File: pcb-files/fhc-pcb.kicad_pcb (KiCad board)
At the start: 2 copper layers, 133.3 x 63.5 mm, 20 parts, among them J1 Screw_Terminal_01x02, SW1 SW_Push_Dual, SW2 SW_Push_Dual, SW3 SW_Push_Dual, SW4 SW_Push_Dual, SW5 SW_Push_Dual, U1 WeMos_D1_mini

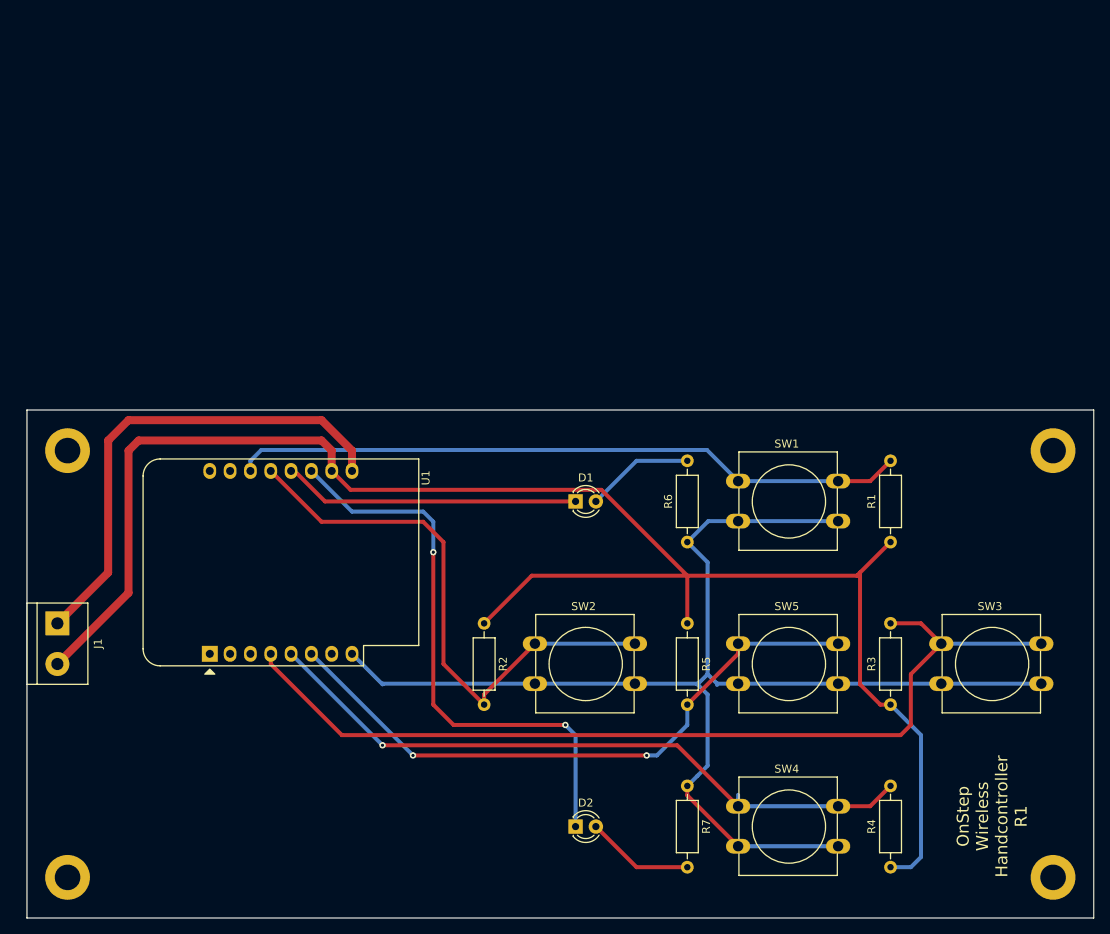
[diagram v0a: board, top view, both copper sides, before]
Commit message: Updated PCB with regulator and 9V battery
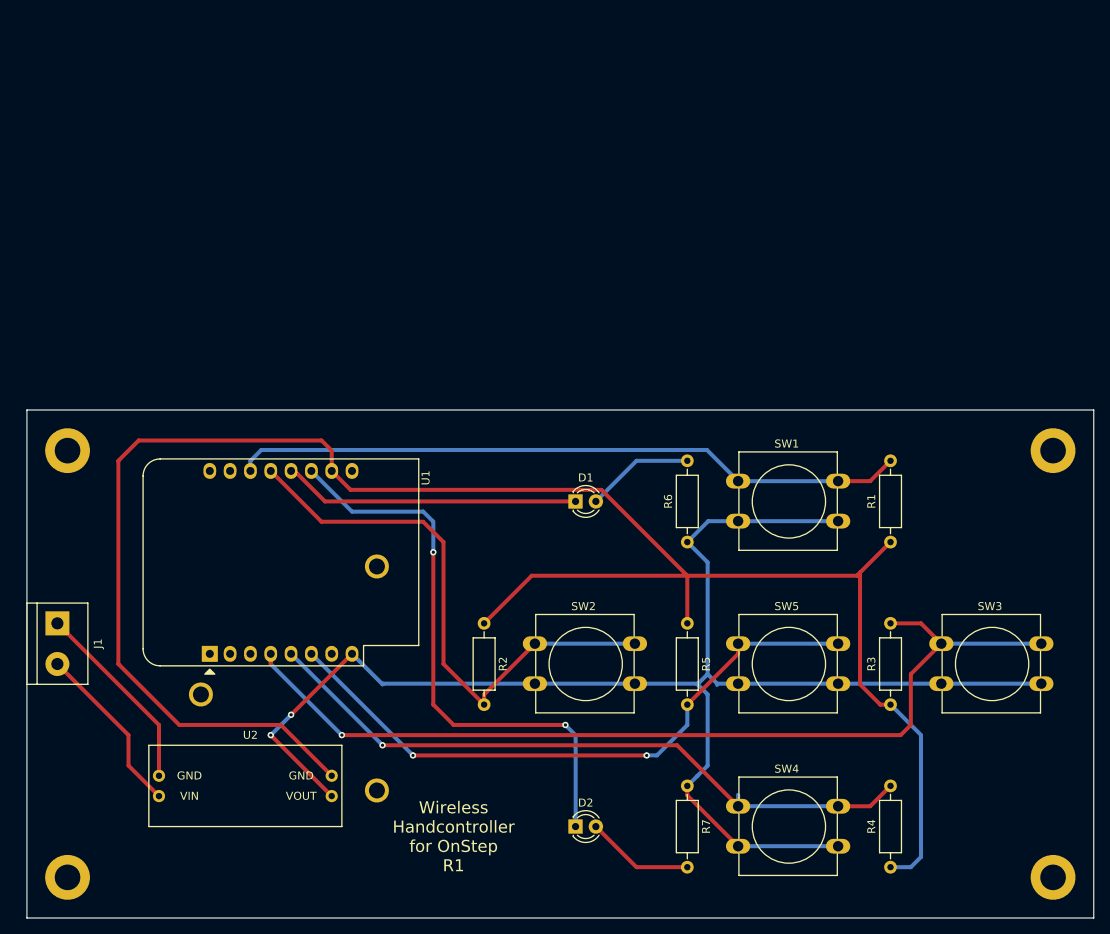
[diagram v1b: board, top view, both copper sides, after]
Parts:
- added REF**: 9V_Batterypack, Personal Library:9V_Batterypack, F.Cu at (127.0, 99.1)
- added U2: AMS1117_Shield_AZDelivery, Personal Library:AMS1117_Shield_AZDelivery, F.Cu at (123.2, 110.5)
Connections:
- J1 pad 1: +5V -> Net-(J1-Pad1)
- J1 pad 2: GND -> Net-(J1-Pad2)
- R1 pad 1: GND -> +9V
- R2 pad 1: GND -> +9V
- R3 pad 1: GND -> +9V
- R4 pad 1: GND -> +9V
- R5 pad 1: GND -> +9V
- U1 pad 10: GND -> +9V
- U1 pad 9: +5V -> Net-(U1-Pad9)
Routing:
- net +9V: track 0.00 -> 243.3 mm
- net GND: track 214.0 -> 0.00 mm
- net +5V: track 61.1 -> 0.00 mm
- net Net-(R6-Pad1): track 163.5 -> 188.6 mm, vias 0 -> 2
- net Net-(J1-Pad1): track 0.00 -> 24.3 mm
- net Net-(J1-Pad2): track 0.00 -> 21.8 mm
- net Net-(R3-Pad2): track 117.1 -> 118.4 mm, vias 0 -> 1
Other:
- board text added: "Wireless Handcontroller for OnStep R1"
- board text removed: "OnStep Wireless Handcontroller R1"

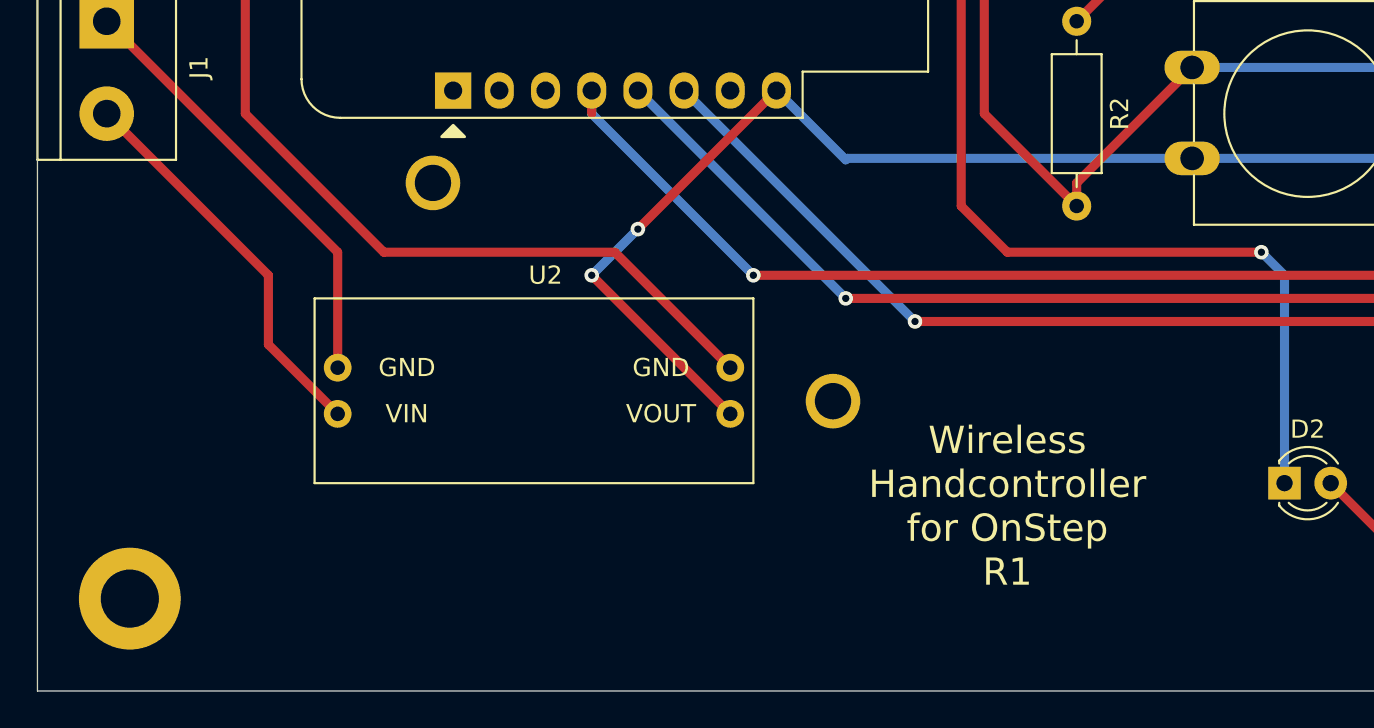
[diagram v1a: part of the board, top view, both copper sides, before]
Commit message: Added power switch
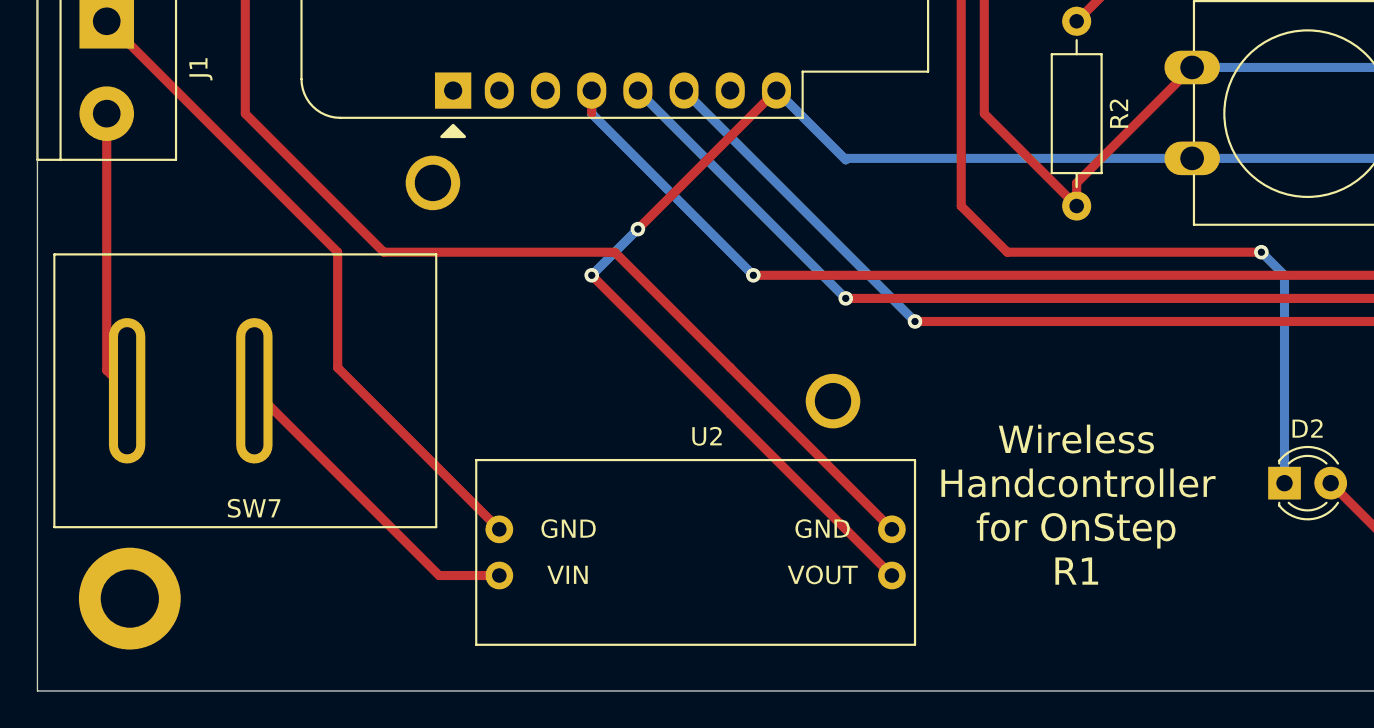
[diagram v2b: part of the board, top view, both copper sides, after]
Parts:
- added SW7: SW_Push, Personal Library:Wippschalter, F.Cu at (106.7, 110.5)
- moved U2 12.6 mm to (132.1, 119.4)
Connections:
- U2 pad 1: Net-(J1-Pad2) -> Net-(SW7-Pad2)
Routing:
- net Net-(SW7-Pad2): track 0.00 -> 17.7 mm
- net Net-(R6-Pad1): track 188.6 -> 201.2 mm
- net +9V: track 243.3 -> 255.9 mm
- net Net-(J1-Pad1): track 24.3 -> 36.9 mm
- net Net-(J1-Pad2): track 21.8 -> 15.7 mm

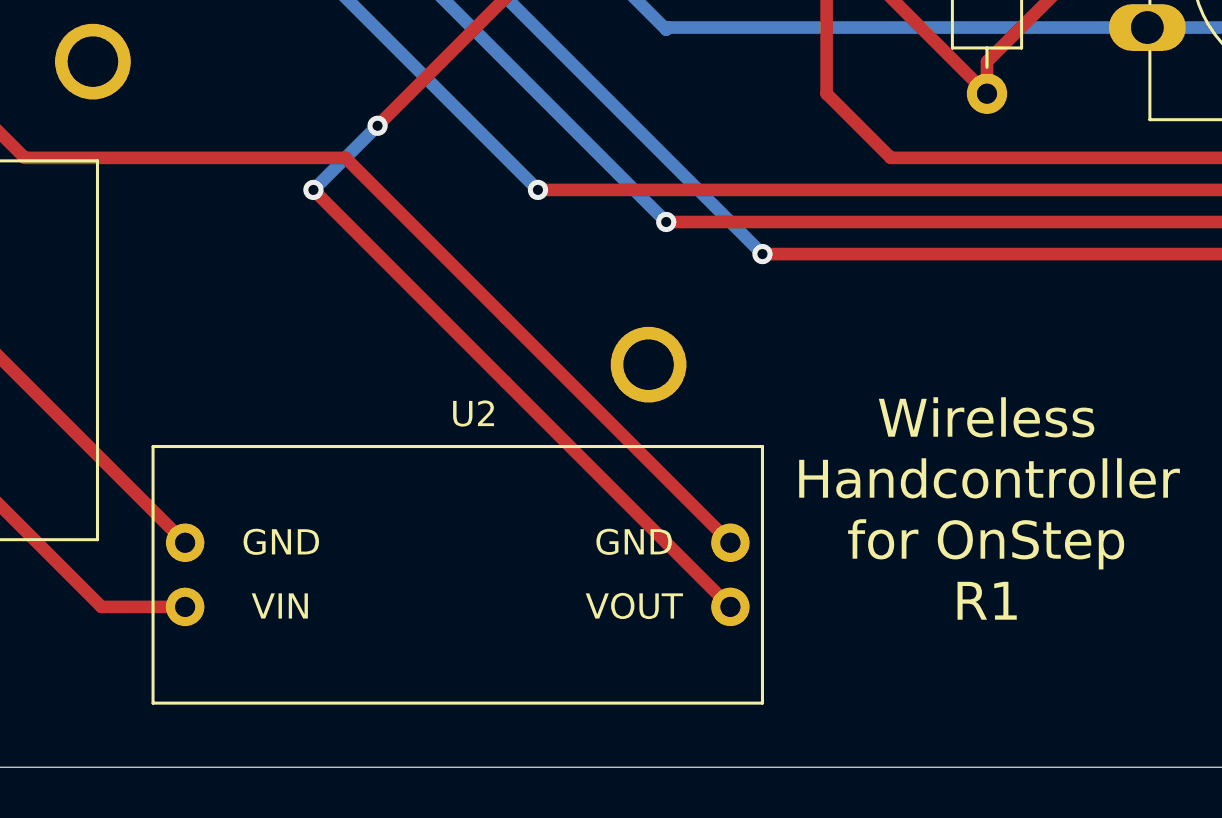
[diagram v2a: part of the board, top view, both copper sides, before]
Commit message: Fixed wrong library reference and pin spacing for AMS1177
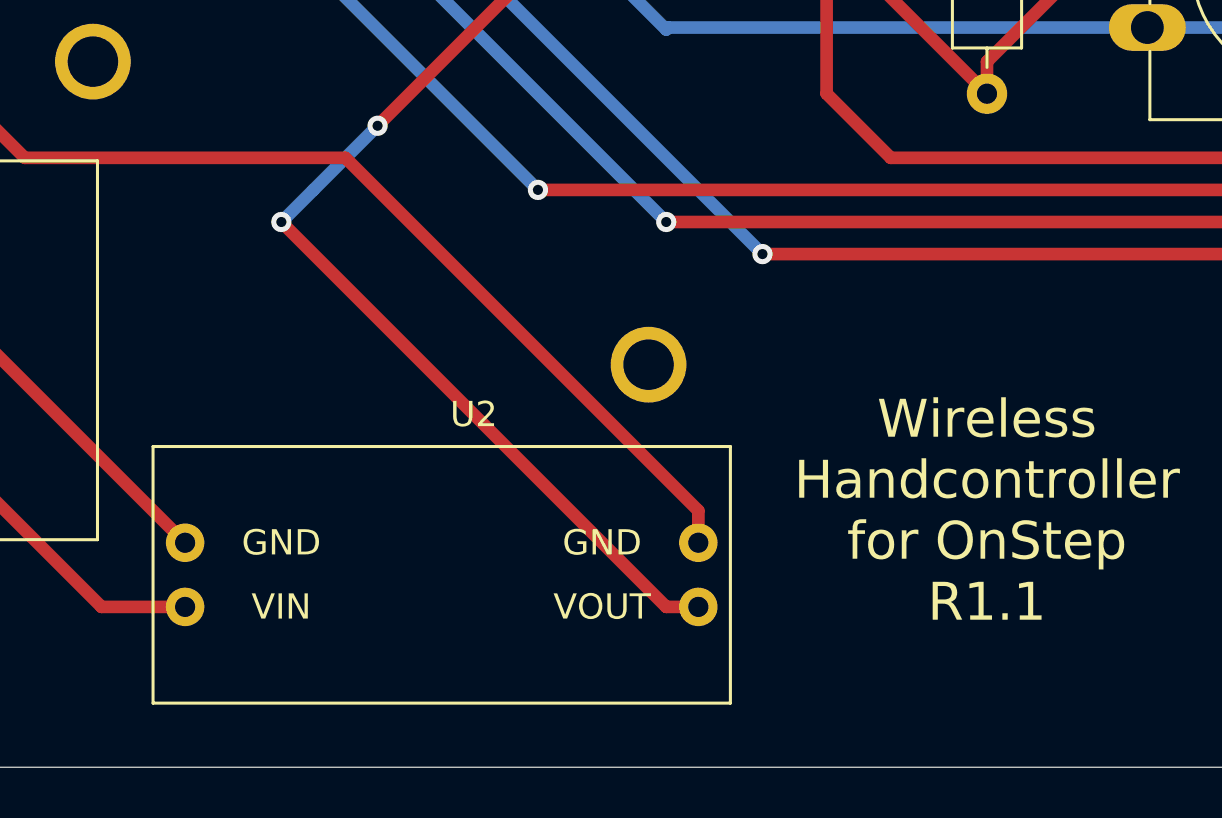
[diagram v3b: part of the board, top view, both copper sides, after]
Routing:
- net Net-(R6-Pad1): track 201.2 -> 202.5 mm
- net +9V: track 255.9 -> 255.3 mm
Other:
- board text added: "Wireless Handcontroller for OnStep R1.1"
- board text removed: "Wireless Handcontroller for OnStep R1"
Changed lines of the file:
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@@
     (thickness 1.6)
     (drawings 7)
-    (tracks 136)
+    (tracks 137)
     (zones 0)
     (modules 23)
@@
     (visible_elements 7FFFFFFF)
     (pcbplotparams
-      (layerselection 0x010fc_ffffffff)
+      (layerselection 0x010f0_ffffffff)
       (usegerberextensions false)
       (usegerberattributes true)
@@
       (outputformat 1)
       (mirror false)
-      (drillshape 1)
+      (drillshape 0)
       (scaleselection 1)
-      (outputdirectory ""))
+      (outputdirectory "C:/Users/Jesco/Desktop/Test_Gerber/"))
   )
   (net 0 "")
@@
     (add_net "Net-(U1-Pad7)")
   )
+  (module "Personal Library:AMS1117_Shield_AZDelivery" (layer F.Cu)
+    (at 132.08 119.38)
+    (fp_text reference U2 (at 0 -6.35) (layer F.SilkS)
+      (effects (font (size 1 1) (thickness 0.15)))
+    )
+    (fp_text value AMS1117_Shield_AZDelivery (at 0 7.62) (layer F.Fab)
+      (effects (font (size 1 1) (thickness 0.15)))
+    )
+    (fp_line (start -12.7 5.08) (end -12.7 -5.08) (layer F.SilkS) (width 0.12))
+    (fp_line (start 10.16 5.08) (end -12.7 5.08) (layer F.SilkS) (width 0.12))
+    (fp_line (start 10.16 -5.08) (end 10.16 5.08) (layer F.SilkS) (width 0.12))
+    (fp_line (start -12.7 -5.08) (end 10.16 -5.08) (layer F.SilkS) (width 0.12))
+    (fp_text user GND (at -7.62 -1.27) (layer F.SilkS)
+      (effects (font (size 1 1) (thickness 0.15)))
+    )
+    (fp_text user GND (at 5.08 -1.27) (layer F.SilkS)
+      (effects (font (size 1 1) (thickness 0.15)))
+    )
+    (fp_text user VOUT (at 5.08 1.27) (layer F.SilkS)
+      (effects (font (size 1 1) (thickness 0.15)))
+    )
+    (fp_text user VIN (at -7.62 1.27) (layer F.SilkS)
+      (effects (font (size 1 1) (thickness 0.15)))
+    )
+    (pad 4 thru_hole circle (at 8.89 1.27) (size 1.524 1.524) (drill 0.8) (layers *.Cu *.Mask)
+      (net 10 "Net-(R6-Pad1)"))
+    (pad 3 thru_hole circle (at 8.89 -1.27) (size 1.524 1.524) (drill 0.8) (layers *.Cu *.Mask)
+      (net 19 +9V))
+    (pad 1 thru_hole circle (at -11.43 1.27) (size 1.524 1.524) (drill 0.8) (layers *.Cu *.Mask)
+      (net 21 "Net-(SW7-Pad2)"))
+    (pad 2 thru_hole circle (at -11.43 -1.27) (size 1.524 1.524) (drill 0.8) (layers *.Cu *.Mask)
+      (net 18 "Net-(J1-Pad1)"))
+  )
   (module "Personal Library:Wippschalter" (layer F.Cu)
     (at 106.68 110.49)
@@
     (pad "" thru_hole circle (at -16 -12 270) (size 3 3) (drill 2) (layers *.Cu *.Mask))
     (pad "" thru_hole circle (at 12 -12 270) (size 3 3) (drill 2) (layers *.Cu *.Mask))
-  )
-  (module "Personal Library:AMS1117_Shield_AZDelivery" (layer F.Cu)
-    (at 132.08 119.38)
-    (fp_text reference U2 (at 0 -6.35) (layer F.SilkS)
-      (effects (font (size 1 1) (thickness 0.15)))
-    )
-    (fp_text value AMS1117_Shield_AZDelivery (at 0 7.62) (layer F.Fab)
-      (effects (font (size 1 1) (thickness 0.15)))
-    )
-    (fp_line (start -12.7 5.08) (end -12.7 -5.08) (layer F.SilkS) (width 0.12))
-    (fp_line (start 11.43 5.08) (end -12.7 5.08) (layer F.SilkS) (width 0.12))
-    (fp_line (start 11.43 -5.08) (end 11.43 5.08) (layer F.SilkS) (width 0.12))
-    (fp_line (start -12.7 -5.08) (end 11.43 -5.08) (layer F.SilkS) (width 0.12))
-    (fp_text user GND (at -7.62 -1.27) (layer F.SilkS)
-      (effects (font (size 1 1) (thickness 0.15)))
-    )
-    (fp_text user GND (at 6.35 -1.27) (layer F.SilkS)
-      (effects (font (size 1 1) (thickness 0.15)))
-    )
-    (fp_text user VOUT (at 6.35 1.27) (layer F.SilkS)
-      (effects (font (size 1 1) (thickness 0.15)))
-    )
-    (fp_text user VIN (at -7.62 1.27) (layer F.SilkS)
-      (effects (font (size 1 1) (thickness 0.15)))
-    )
-    (pad 4 thru_hole circle (at 10.16 1.27) (size 1.524 1.524) (drill 0.8) (layers *.Cu *.Mask)
-      (net 10 "Net-(R6-Pad1)"))
-    (pad 3 thru_hole circle (at 10.16 -1.27) (size 1.524 1.524) (drill 0.8) (layers *.Cu *.Mask)
-      (net 19 +9V))
-    (pad 1 thru_hole circle (at -11.43 1.27) (size 1.524 1.524) (drill 0.8) (layers *.Cu *.Mask)
-      (net 21 "Net-(SW7-Pad2)"))
-    (pad 2 thru_hole circle (at -11.43 -1.27) (size 1.524 1.524) (drill 0.8) (layers *.Cu *.Mask)
-      (net 18 "Net-(J1-Pad1)"))
   )
   (module MountingHole:MountingHole_3.2mm_M3_DIN965_Pad (layer F.Cu)
@@
   (gr_line (start 228.6 63.5) (end 228.6 127) (layer Edge.Cuts) (width 0.05))
   (gr_line (start 95.25 63.5) (end 228.6 63.5) (layer Edge.Cuts) (width 0.05))
-  (gr_text "Wireless \nHandcontroller\nfor OnStep\nR1" (at 152.4 116.84) (layer F.SilkS)
+  (gr_text "Wireless \nHandcontroller\nfor OnStep\nR1.1" (at 152.4 116.84) (layer F.SilkS)
     (effects (font (size 1.5 1.5) (thickness 0.3)))
   )
@@
   (segment (start 181.53 97.71) (end 181.53 97.87) (width 0.5) (layer B.Cu) (net 10))
   (segment (start 196.65 97.71) (end 209.55 97.71) (width 0.5) (layer B.Cu) (net 10))
-  (segment (start 125.73 104.14) (end 125.73 104.14) (width 0.5) (layer F.Cu) (net 10))
-  (via (at 125.73 104.14) (size 0.8) (drill 0.4) (layers F.Cu B.Cu) (net 10))
   (segment (start 125.73 104.14) (end 128.27 101.6) (width 0.5) (layer B.Cu) (net 10))
   (segment (start 128.27 101.6) (end 128.27 101.6) (width 0.5) (layer B.Cu) (net 10))
   (via (at 128.27 101.6) (size 0.8) (drill 0.4) (layers F.Cu B.Cu) (net 10))
   (segment (start 128.27 101.6) (end 135.89 93.98) (width 0.5) (layer F.Cu) (net 10))
-  (segment (start 142.24 120.65) (end 133.35 111.76) (width 0.5) (layer F.Cu) (net 10))
-  (segment (start 133.35 111.76) (end 125.73 104.14) (width 0.5) (layer F.Cu) (net 10))
+  (segment (start 140.97 120.65) (end 139.7 120.65) (width 0.5) (layer F.Cu) (net 10))
+  (segment (start 139.7 120.65) (end 124.46 105.41) (width 0.5) (layer F.Cu) (net 10))
+  (segment (start 125.73 104.14) (end 124.46 105.41) (width 0.5) (layer B.Cu) (net 10))
+  (segment (start 124.46 105.41) (end 124.46 105.41) (width 0.5) (layer B.Cu) (net 10))
+  (via (at 124.46 105.41) (size 0.8) (drill 0.4) (layers F.Cu B.Cu) (net 10))
   (segment (start 99.06 109.37) (end 100.18 110.49) (width 0.5) (layer F.Cu) (net 17))
   (segment (start 99.06 95.25) (end 99.06 109.37) (width 0.5) (layer F.Cu) (net 17))
@@
   (segment (start 207.01 104.14) (end 207.01 119.38) (width 0.5) (layer B.Cu) (net 19))
   (segment (start 203.2 100.33) (end 207.01 104.14) (width 0.5) (layer B.Cu) (net 19))
+  (segment (start 140.97 116.84) (end 140.97 118.11) (width 0.5) (layer F.Cu) (net 19))
   (segment (start 106.68 95.25) (end 114.3 102.87) (width 0.5) (layer F.Cu) (net 19))
   (segment (start 106.68 69.85) (end 106.68 95.25) (width 0.5) (layer F.Cu) (net 19))
@@
   (segment (start 132.08 67.31) (end 109.22 67.31) (width 0.5) (layer F.Cu) (net 19))
   (segment (start 133.35 68.58) (end 132.08 67.31) (width 0.5) (layer F.Cu) (net 19))
+  (segment (start 127 102.87) (end 140.97 116.84) (width 0.5) (layer F.Cu) (net 19))
   (segment (start 114.3 102.87) (end 127 102.87) (width 0.5) (layer F.Cu) (net 19))
   (segment (start 133.35 71.12) (end 133.35 68.58) (width 0.5) (layer F.Cu) (net 19))
-  (segment (start 127 102.87) (end 133.35 109.22) (width 0.5) (layer F.Cu) (net 19))
-  (segment (start 133.35 109.22) (end 142.24 118.11) (width 0.5) (layer F.Cu) (net 19))
   (segment (start 120.65 120.65) (end 117.34 120.65) (width 0.5) (layer F.Cu) (net 21))
   (segment (start 117.34 120.65) (end 107.18 110.49) (width 0.5) (layer F.Cu) (net 21))
